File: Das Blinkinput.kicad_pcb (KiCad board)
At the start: 4 copper layers, 25.4 x 50.8 mm, 33 parts, among them P101 CONN_01X02, P102 CONN_01X01, P103 CONN_01X01, P104 CONN_01X01, P105 CONN_01X05, P201 CONN_01X01, P301 CONN_01X01, P401 CONN_01X01, P501 CONN_01X01, U101 LP2980IM5-3.0/NOPB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

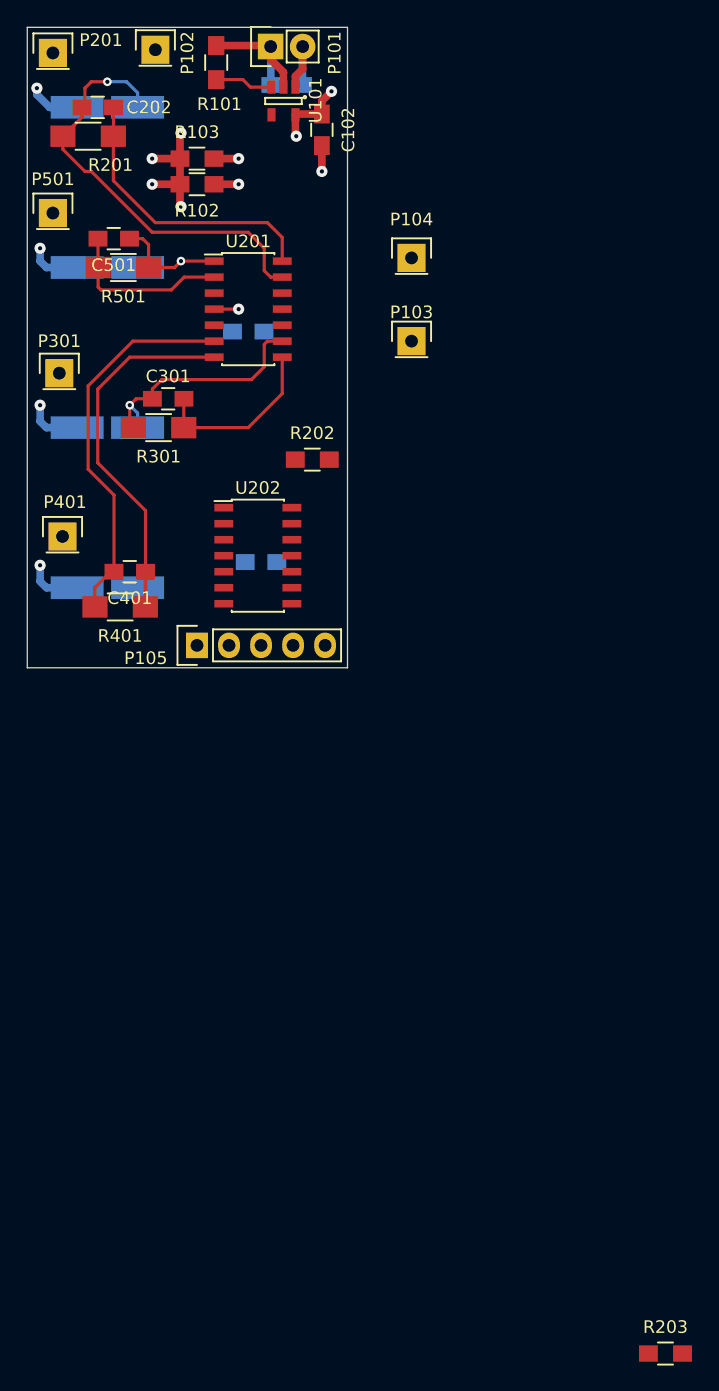
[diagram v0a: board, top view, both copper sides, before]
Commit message: Routed remainder of lines and added test points with lables
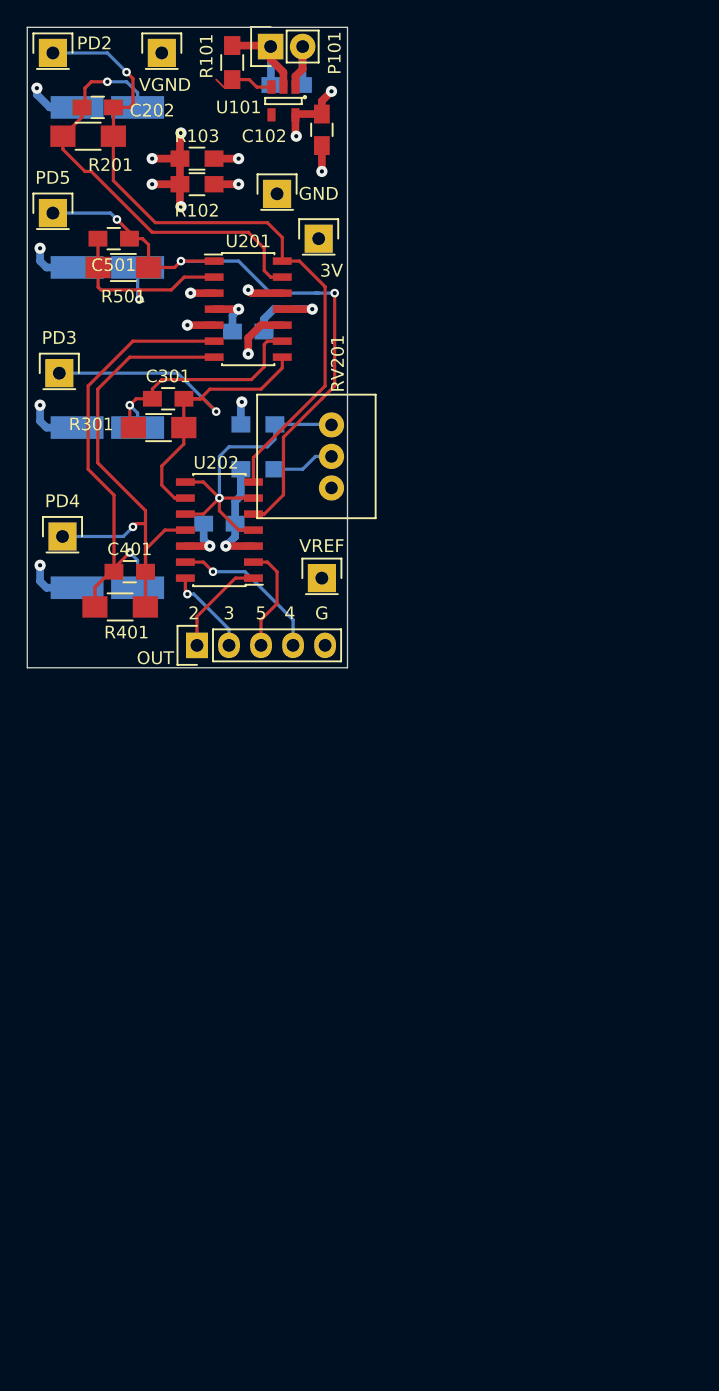
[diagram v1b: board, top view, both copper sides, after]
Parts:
- added P106: CONN_01X01, Pin_Headers:Pin_Header_Straight_1x01, F.Cu at (101.3, 111.3)
- added RV201: POT, Current:P090L-02F25BR10K, F.Cu at (102.1, 101.6)
- R202, R203: moved to B.Cu
- moved R203 77.2 mm to (96.3, 102.6), turned to 180 degrees
- moved P104 11.8 mm to (97.8, 80.8)
- moved P103 11.0 mm to (101.1, 84.3)
- moved R202 5.14 mm to (96.3, 99.1)
- moved C203 4.49 mm to (93.2, 106.9), turned to 0 degrees
- moved U202 3.66 mm to (93.2, 107.4), turned to 180 degrees
- moved R101 1.27 mm to (94.2, 70.4)
- moved P102 0.57 mm to (88.6, 69.6)
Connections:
- net /Channel4Photodetect/Channel4_Out renamed /Channel4Photodetect/PD4
- P105 pad 1: /Channel1Photodetect/Channel1_Out -> /Channel1Photodetect/PD2
- P105 pad 2: /Channel2Photodetect/Channel2_Out -> /Channel2Photodetect/PD3
- P105 pad 3: /Channel3Photodetect/Channel3_Out -> /Channel3Photodetect/PD5
- U202 pad 1: /Channel2Photodetect/Channel2_Out -> /Channel1Photodetect/PD2
- U202 pad 14: /Channel3Photodetect/Channel3_Out -> /Channel2Photodetect/PD3
- U202 pad 2: /Channel1Photodetect/Channel1_Out -> /Channel3Photodetect/PD5
- U202 pad 5: Net-(C202-Pad1) -> Net-(C501-Pad1)
- U202 pad 7: Net-(C301-Pad1) -> Net-(C202-Pad1)
- U202 pad 9: Net-(C501-Pad1) -> Net-(C301-Pad1)
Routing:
- net Net-(C501-Pad1): track 8.94 -> 50.4 mm, vias 1 -> 3
- net Net-(C202-Pad1): track 23.0 -> 55.9 mm, vias 0 -> 1
- net /Channel2Photodetect/REF_IN: track 0.00 -> 27.5 mm, vias 0 -> 1
- net Net-(C301-Pad1): track 14.1 -> 36.2 mm, vias 0 -> 1
- net Net-(C401-Pad1): track 29.1 -> 41.7 mm, vias 0 -> 1
- net /Channel4Photodetect/PD4: track 0.00 -> 12.5 mm, vias 0 -> 1
- net GND: track 15.1 -> 27.2 mm, vias 2 -> 5
- net VGND: track 27.4 -> 38.6 mm, vias 8 -> 12
- net 3V: track 9.85 -> 20.6 mm, vias 4 -> 5
- net /Channel3Photodetect/PD5: track 0.00 -> 8.56 mm
- net /Channel1Photodetect/PD2: track 0.00 -> 8.03 mm
- net /Channel2Photodetect/PD3: track 0.00 -> 7.07 mm, vias 0 -> 1
- net Net-(C401-Pad2): track 30.6 -> 35.7 mm, vias 0 -> 1
- net Net-(R203-Pad1): track 0.00 -> 4.91 mm
- net Net-(C501-Pad2): track 13.6 -> 16.9 mm, vias 0 -> 1
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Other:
- board text added: "2"
- board text added: "3"
- board text added: "3V"
- board text added: "4"
- board text added: "5"
- board text added: "G"
- board text added: "GND"
- board text added: "OUT"
- board text added: "PD2"
- board text added: "PD3"
- board text added: "PD4"
- board text added: "PD5"
- board text added: "VGND"
- board text added: "VREF"

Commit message: Connected REF_IN Test Point
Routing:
- net /Channel2Photodetect/REF_IN: track 27.5 -> 35.2 mm

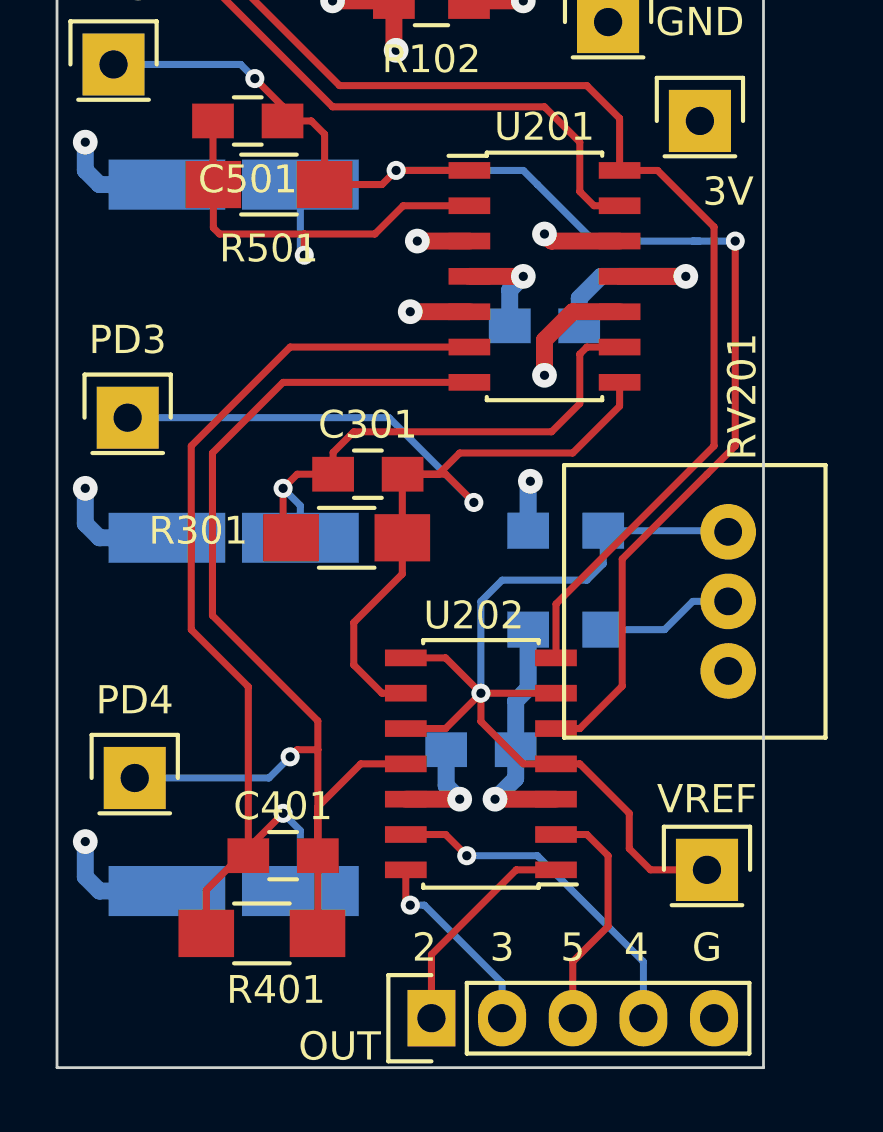
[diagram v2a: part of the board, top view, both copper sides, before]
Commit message: Moved potentiometer and output pins
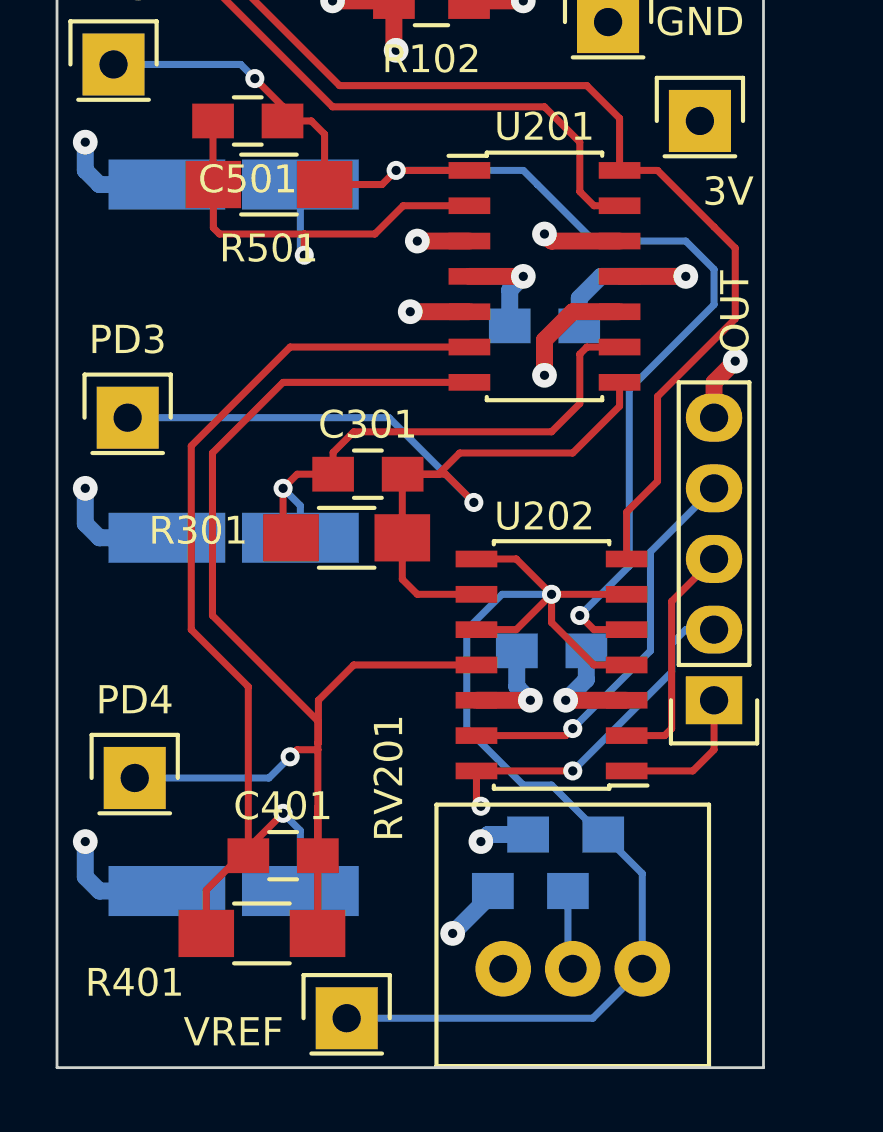
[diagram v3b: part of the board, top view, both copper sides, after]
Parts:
- moved P105 15.3 mm to (101.6, 105.2), turned to 180 degrees
- moved RV201 14.3 mm to (96.5, 114.8), turned to 0 degrees
- moved P106 14.0 mm to (88.4, 116.6)
- moved R202 10.9 mm to (96.3, 110.0)
- moved R203 9.48 mm to (95.0, 112.0)
- moved C203 4.37 mm to (95.8, 103.4)
- moved U202 4.37 mm to (95.8, 103.9)
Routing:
- net /Channel2Photodetect/REF_IN: track 35.2 -> 43.9 mm
- net /Channel2Photodetect/PD3: track 7.07 -> 12.6 mm, vias 1 -> 2
- net Net-(C501-Pad1): track 50.4 -> 45.4 mm
- net Net-(C202-Pad1): track 55.9 -> 51.9 mm
- net Net-(C401-Pad1): track 41.7 -> 45.7 mm
- net Net-(C301-Pad1): track 36.2 -> 33.0 mm
- net /Channel1Photodetect/PD2: track 8.03 -> 5.24 mm
- net 3V: track 20.6 -> 18.2 mm, vias 5 -> 6
- net GND: track 27.2 -> 29.5 mm, vias 5 -> 6
- net Net-(R203-Pad1): track 4.91 -> 2.87 mm
- net /Channel4Photodetect/PD4: track 12.5 -> 14.3 mm

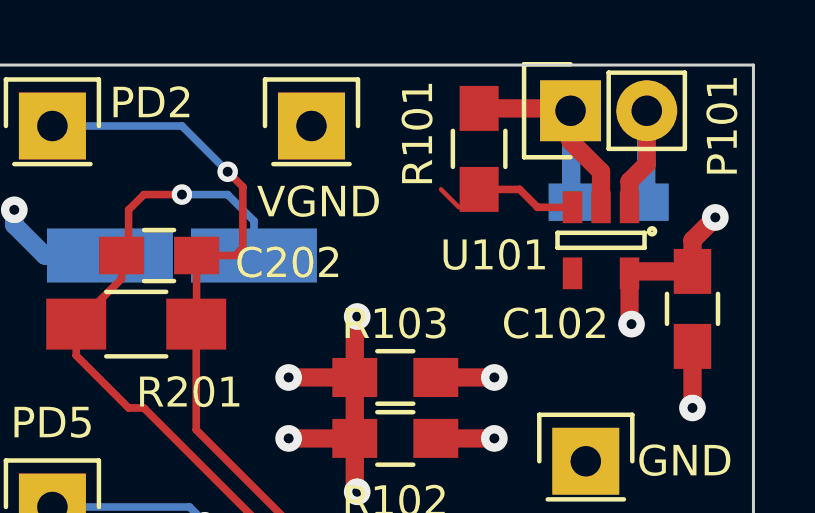
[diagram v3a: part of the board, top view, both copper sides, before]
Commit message: Added CE logo and did DRC
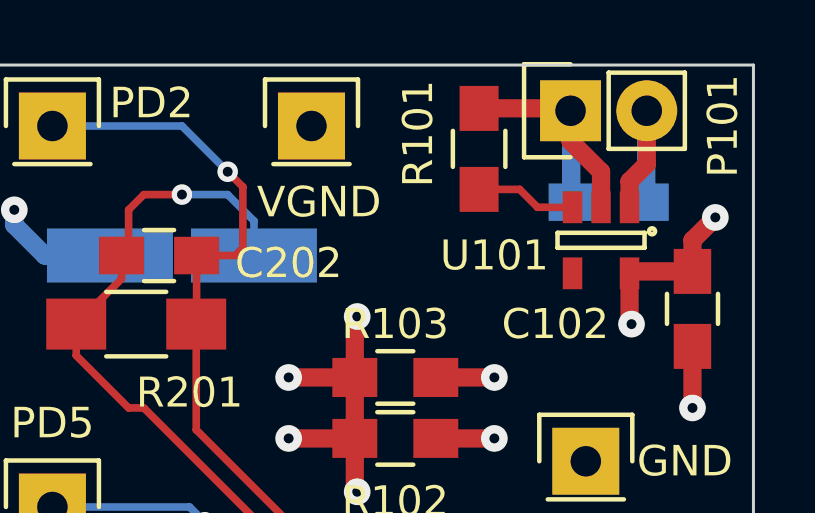
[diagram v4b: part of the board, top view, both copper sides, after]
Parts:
- added G***: LOGO, DasBlinkinput:CE_logo, B.Cu at (92.2, 78.2)
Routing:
- net (no net): track 0.85 -> 0.00 mm
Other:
- board text added: "DasBlinkinput Ver 1.0"
